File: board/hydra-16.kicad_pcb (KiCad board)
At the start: 2 copper layers, 304.8 x 243.8 mm, 171 parts, among them IC1 74LS189, IC2 74LS189, IC3 74LS189, IC4 74LS189, IC5 74LS219, IC6 74LS219, IC7 74LS219, IC8 74LS219, J1 Conn_01x32, J10 SLOT 1, J11 SLOT 2, J12 SLOT 3, J13 SLOT 4, J14 SLOT 5, J15 AudioJack3, J16 SPI Device 0, J17 Front Panel, J18 SPI Device 1, J19 SPI Device 2, J2 Conn_01x24, J20 SPI Device 3, J21 SPI Device 4, J22 SPI Device 5, J23 SPI Device 6, J24 SPI Device 7, J3 DE9_Plug, J4 7.15909MHz, J5 ATX-24, J6 0.89489MHz, J7 1.78977MHz, J8 3.57955MHz, J9 SLOT 0, U1 74F573, U10 74LS154, U11 74F00, U12 74F86, U13 74F08, U14 74F32, U15 74F30, U16 74LS260, U17 74LS154, U18 74F04, U19 HM628512LP-5, U2 74F541, U20 HM628512LP-5, U21 HM628512LP-5, U22 HM628512LP-5, U23 74F139, U24 74F20, U25 74F02, U26 74LS154, U27 74F138, U28 AT29C040, U29 AT29C040, U3 AT28C64B, U30 AT29C040, U31 AT29C040, U32 AT29C040, U33 AT29C040, U34 AT29C040, U35 AT29C040, U36 74ACT14, U37 74F191, U38 TL074, U39 YM2151, U4 W65C02SxP, U40 YM3012, U41 DM1813-10, U42 74F157, U43 74F157, U44 74LS148, U45 74LS148, U46 74F32, U47 74F573, U48 74F541, U49 74F573, U5 6522, U50 74F541, U51 74F32, U52 74F04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

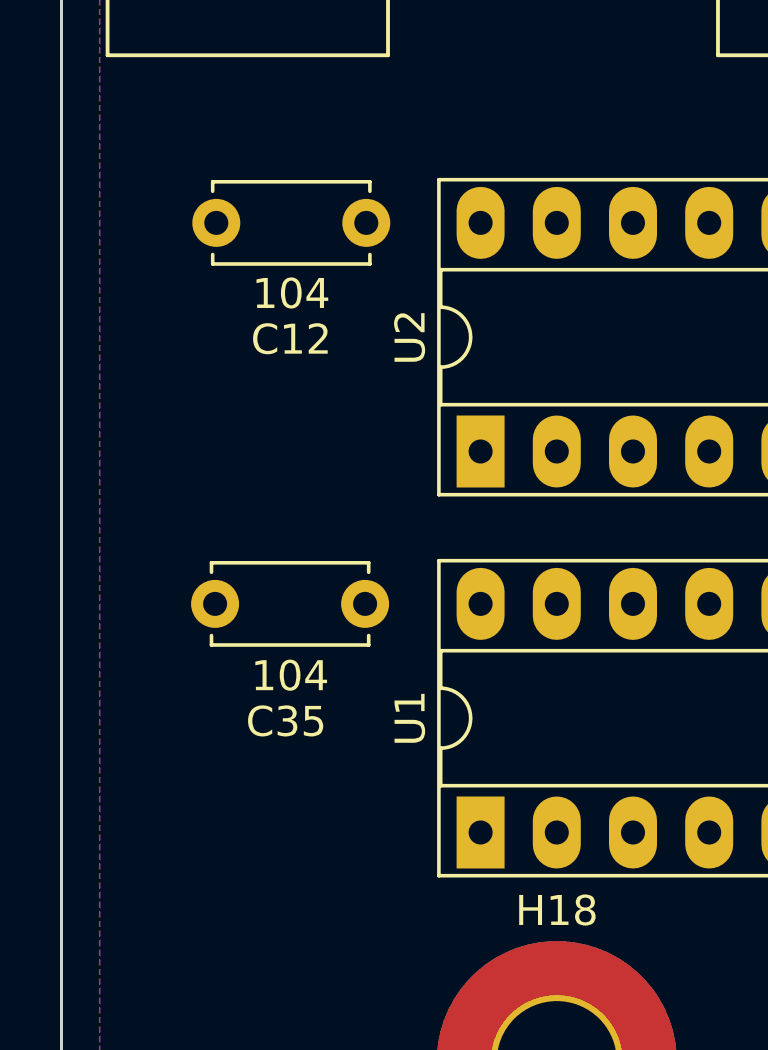
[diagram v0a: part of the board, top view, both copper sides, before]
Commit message: Cap position tweaks.
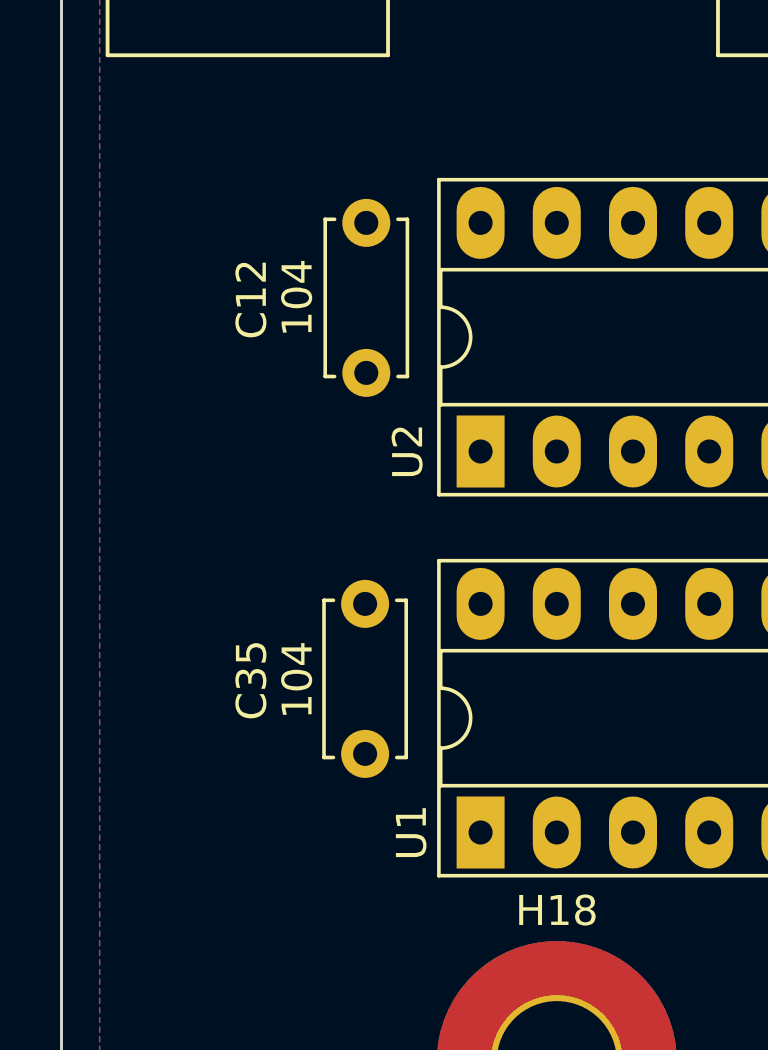
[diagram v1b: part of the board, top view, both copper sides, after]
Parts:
- turned C12 to -90 degrees
- turned C35 to -90 degrees
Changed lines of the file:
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@@
 		(tags "THT DIP DIL PDIP 2.54mm 7.62mm 300mil Socket LongPads")
 		(property "Reference" "U2"
-			(at 3.81 -2.33 90)
+			(at 0 -2.413 90)
 			(layer "F.SilkS")
 			(effects
@@
 	(footprint "Capacitor_THT:C_Disc_D5.0mm_W2.5mm_P5.00mm"
 		(layer "F.Cu")
-		(at -294.64 137.16 180)
+		(at -294.64 137.16 -90)
 		(descr "C, Disc series, Radial, pin pitch=5.00mm, , diameter*width=5*2.5mm^2, Capacitor, http://cdn-reichelt.de/documents/datenblatt/B300/DS_KERKO_TC.pdf")
 		(tags "C Disc series Radial pin pitch 5.00mm  diameter 5mm width 2.5mm Capacitor")
 		(property "Reference" "C12"
-			(at 2.5 -3.897 0)
+			(at 2.54 3.81 90)
 			(layer "F.SilkS")
 			(effects
@@
 		)
 		(property "Value" "104"
-			(at 2.5 -2.373 0)
+			(at 2.5 2.286 90)
 			(layer "F.SilkS")
 			(effects
@@
 		)
 		(property "Footprint" "Capacitor_THT:C_Disc_D5.0mm_W2.5mm_P5.00mm"
-			(at 0 0 180)
+			(at 0 0 -90)
 			(unlocked yes)
 			(layer "F.Fab")
@@
 		)
 		(property "Datasheet" ""
-			(at 0 0 180)
+			(at 0 0 -90)
 			(unlocked yes)
 			(layer "F.Fab")
@@
 		)
 		(property "Description" "Unpolarized capacitor, small symbol"
-			(at 0 0 180)
+			(at 0 0 -90)
 			(unlocked yes)
 			(layer "F.Fab")
@@
 		(attr through_hole)
 		(fp_line
-			(start 5.12 1.055)
+			(start -0.12 1.37)
 			(end 5.12 1.37)
 			(stroke
@@
 		)
 		(fp_line
-			(start 5.12 -1.37)
-			(end 5.12 -1.055)
+			(start -0.12 1.055)
+			(end -0.12 1.37)
 			(stroke
 				(width 0.12)
@@
 		)
 		(fp_line
-			(start -0.12 1.37)
+			(start 5.12 1.055)
 			(end 5.12 1.37)
 			(stroke
@@
 		)
 		(fp_line
-			(start -0.12 1.055)
-			(end -0.12 1.37)
+			(start -0.12 -1.37)
+			(end -0.12 -1.055)
 			(stroke
 				(width 0.12)
@@
 		)
 		(fp_line
-			(start -0.12 -1.37)
-			(end -0.12 -1.055)
+			(start 5.12 -1.37)
+			(end 5.12 -1.055)
 			(stroke
 				(width 0.12)
@@
 		)
 		(fp_line
-			(start 6.05 1.5)
-			(end 6.05 -1.5)
+			(start -1.05 1.5)
+			(end 6.05 1.5)
 			(stroke
 				(width 0.05)
@@
 		)
 		(fp_line
-			(start 6.05 -1.5)
-			(end -1.05 -1.5)
+			(start 6.05 1.5)
+			(end 6.05 -1.5)
 			(stroke
 				(width 0.05)
@@
 		)
 		(fp_line
-			(start -1.05 1.5)
-			(end 6.05 1.5)
+			(start -1.05 -1.5)
+			(end -1.05 1.5)
 			(stroke
 				(width 0.05)
@@
 		)
 		(fp_line
-			(start -1.05 -1.5)
-			(end -1.05 1.5)
+			(start 6.05 -1.5)
+			(end -1.05 -1.5)
 			(stroke
 				(width 0.05)
@@
 		)
 		(fp_line
-			(start 5 1.25)
-			(end 5 -1.25)
+			(start 0 1.25)
+			(end 5 1.25)
 			(stroke
 				(width 0.1)
@@
 		)
 		(fp_line
-			(start 5 -1.25)
-			(end 0 -1.25)
+			(start 5 1.25)
+			(end 5 -1.25)
 			(stroke
 				(width 0.1)
@@
 		)
 		(fp_line
-			(start 0 1.25)
-			(end 5 1.25)
+			(start 0 -1.25)
+			(end 0 1.25)
 			(stroke
 				(width 0.1)
@@
 		)
 		(fp_line
-			(start 0 -1.25)
-			(end 0 1.25)
+			(start 5 -1.25)
+			(end 0 -1.25)
 			(stroke
 				(width 0.1)
@@
 		)
 		(fp_text user "${REFERENCE}"
-			(at 2.5 0 0)
+			(at 2.5 0 90)
 			(layer "F.Fab")
 			(effects
@@
 		)
 		(pad "1" thru_hole circle
-			(at 0 0 180)
+			(at 0 0 270)
 			(size 1.6 1.6)
 			(drill 0.8)
@@
 		)
 		(pad "2" thru_hole circle
-			(at 5 0 180)
+			(at 5 0 270)
 			(size 1.6 1.6)
 			(drill 0.8)
@@
 		(tags "THT DIP DIL PDIP 2.54mm 7.62mm 300mil Socket LongPads")
 		(property "Reference" "U1"
-			(at 3.81 -2.33 90)
+			(at 0 -2.286 90)
 			(layer "F.SilkS")
 			(effects
@@
 	(footprint "Capacitor_THT:C_Disc_D5.0mm_W2.5mm_P5.00mm"
 		(layer "F.Cu")
-		(at -294.68 149.86 180)
+		(at -294.68 149.86 -90)
 		(descr "C, Disc series, Radial, pin pitch=5.00mm, , diameter*width=5*2.5mm^2, Capacitor, http://cdn-reichelt.de/documents/datenblatt/B300/DS_KERKO_TC.pdf")
 		(tags "C Disc series Radial pin pitch 5.00mm  diameter 5mm width 2.5mm Capacitor")
 		(property "Reference" "C35"
-			(at 2.627 -3.937 0)
+			(at 2.54 3.77 90)
 			(layer "F.SilkS")
 			(effects
@@
 		)
 		(property "Value" "104"
-			(at 2.5 -2.413 0)
+			(at 2.54 2.246 90)
 			(layer "F.SilkS")
 			(effects
@@
 		)
 		(property "Footprint" "Capacitor_THT:C_Disc_D5.0mm_W2.5mm_P5.00mm"
-			(at 0 0 180)
+			(at 0 0 -90)
 			(unlocked yes)
 			(layer "F.Fab")
@@
 		)
 		(property "Datasheet" ""
-			(at 0 0 180)
+			(at 0 0 -90)
 			(unlocked yes)
 			(layer "F.Fab")
@@
 		)
 		(property "Description" "Unpolarized capacitor, small symbol"
-			(at 0 0 180)
+			(at 0 0 -90)
 			(unlocked yes)
 			(layer "F.Fab")
@@
 		(attr through_hole)
 		(fp_line
-			(start 5.12 1.055)
+			(start -0.12 1.37)
 			(end 5.12 1.37)
 			(stroke
@@
 		)
 		(fp_line
-			(start 5.12 -1.37)
-			(end 5.12 -1.055)
+			(start -0.12 1.055)
+			(end -0.12 1.37)
 			(stroke
 				(width 0.12)
@@
 		)
 		(fp_line
-			(start -0.12 1.37)
+			(start 5.12 1.055)
 			(end 5.12 1.37)
 			(stroke
@@
 		)
 		(fp_line
-			(start -0.12 1.055)
-			(end -0.12 1.37)
+			(start -0.12 -1.37)
+			(end -0.12 -1.055)
 			(stroke
 				(width 0.12)
@@
 		)
 		(fp_line
-			(start -0.12 -1.37)
-			(end -0.12 -1.055)
+			(start 5.12 -1.37)
+			(end 5.12 -1.055)
 			(stroke
 				(width 0.12)
@@
 		)
 		(fp_line
-			(start 6.05 1.5)
-			(end 6.05 -1.5)
+			(start -1.05 1.5)
+			(end 6.05 1.5)
 			(stroke
 				(width 0.05)
@@
 		)
 		(fp_line
-			(start 6.05 -1.5)
-			(end -1.05 -1.5)
+			(start 6.05 1.5)
+			(end 6.05 -1.5)
 			(stroke
 				(width 0.05)
@@
 		)
 		(fp_line
-			(start -1.05 1.5)
-			(end 6.05 1.5)
+			(start -1.05 -1.5)
+			(end -1.05 1.5)
 			(stroke
 				(width 0.05)
@@
 		)
 		(fp_line
-			(start -1.05 -1.5)
-			(end -1.05 1.5)
+			(start 6.05 -1.5)
+			(end -1.05 -1.5)
 			(stroke
 				(width 0.05)
@@
 		)
 		(fp_line
-			(start 5 1.25)
-			(end 5 -1.25)
+			(start 0 1.25)
+			(end 5 1.25)
 			(stroke
 				(width 0.1)
@@
 		)
 		(fp_line
-			(start 5 -1.25)
-			(end 0 -1.25)
+			(start 5 1.25)
+			(end 5 -1.25)
 			(stroke
 				(width 0.1)
@@
 		)
 		(fp_line
-			(start 0 1.25)
-			(end 5 1.25)
+			(start 0 -1.25)
+			(end 0 1.25)
 			(stroke
 				(width 0.1)
@@
 		)
 		(fp_line
-			(start 0 -1.25)
-			(end 0 1.25)
+			(start 5 -1.25)
+			(end 0 -1.25)
 			(stroke
 				(width 0.1)
@@
 		)
 		(fp_text user "${REFERENCE}"
-			(at 2.5 0 0)
+			(at 2.5 0 90)
 			(layer "F.Fab")
 			(effects
@@
 		)
 		(pad "1" thru_hole circle
-			(at 0 0 180)
+			(at 0 0 270)
 			(size 1.6 1.6)
 			(drill 0.8)
@@
 		)
 		(pad "2" thru_hole circle
-			(at 5 0 180)
+			(at 5 0 270)
 			(size 1.6 1.6)
 			(drill 0.8)

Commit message: More PCB position tweaks.
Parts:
- RN2: value 3.3k -> 332
- U4: value W65C02SxP -> W65C02S
- U5: value 6522 -> 65C22
- U6: value 6551 -> 65C51
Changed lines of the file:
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@@
 		(tags "THT DIP DIL PDIP 2.54mm 7.62mm 300mil Socket LongPads")
 		(property "Reference" "IC2"
-			(at -0.1455 -2.4839 180)
+			(at 3.7915 21.7731 180)
 			(layer "F.SilkS")
 			(effects
@@
 			)
 		)
-		(property "Value" "W65C02SxP"
+		(property "Value" "W65C02S"
 			(at 7.62 50.59 180)
 			(layer "F.SilkS")
@@
 			)
 		)
-		(property "Value" "6551"
+		(property "Value" "65C51"
 			(at 7.62 35.35 0)
 			(layer "F.SilkS")
@@
 		(tags "THT DIP DIL PDIP 2.54mm 7.62mm 300mil Socket LongPads")
 		(property "Reference" "U23"
-			(at -0.381 -2.667 0)
+			(at 3.673 21.854 0)
 			(layer "F.SilkS")
 			(effects
@@
 		(tags "R")
 		(property "Reference" "RN2"
-			(at -2.794 0 180)
+			(at -4.064 0 180)
 			(layer "F.SilkS")
 			(effects
@@
 			)
 		)
-		(property "Value" "3.3k"
-			(at 22.86 0 180)
+		(property "Value" "332"
+			(at -2.54 0 180)
 			(layer "F.SilkS")
 			(effects
@@
 		(tags "R")
 		(property "Reference" "RN3"
-			(at -2.794 0 180)
+			(at -4.064 0 180)
 			(layer "F.SilkS")
 			(effects
@@
 		)
 		(property "Value" "332"
-			(at 22.86 0 180)
+			(at -2.54 0 180)
 			(layer "F.SilkS")
 			(effects
@@
 		(tags "R")
 		(property "Reference" "RN1"
-			(at 11.43 4.064 90)
+			(at 10.16 4.064 90)
 			(layer "F.SilkS")
 			(effects
@@
 		)
 		(property "Value" "332"
-			(at 11.43 2.413 90)
+			(at 10.16 2.413 90)
 			(layer "F.SilkS")
 			(effects
@@
 			)
 		)
-		(property "Value" "6522"
+		(property "Value" "65C22"
 			(at 7.62 50.59 180)
 			(layer "F.SilkS")

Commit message: More PCB position tweaks.
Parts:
- turned C41 to 0 degrees
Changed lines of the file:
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@@
 	(footprint "Capacitor_THT:C_Disc_D5.0mm_W2.5mm_P5.00mm"
 		(layer "F.Cu")
-		(at -261.62 138.43 90)
+		(at -261.62 138.43)
 		(descr "C, Disc series, Radial, pin pitch=5.00mm, , diameter*width=5*2.5mm^2, Capacitor, http://cdn-reichelt.de/documents/datenblatt/B300/DS_KERKO_TC.pdf")
 		(tags "C Disc series Radial pin pitch 5.00mm  diameter 5mm width 2.5mm Capacitor")
 		(property "Reference" "C41"
-			(at 2.413 3.81 90)
+			(at 2.413 -3.81 360)
 			(layer "F.SilkS")
 			(effects
@@
 		)
 		(property "Value" "104"
-			(at 2.54 2.286 90)
+			(at 2.54 -2.286 360)
 			(layer "F.SilkS")
 			(effects
@@
 		)
 		(property "Footprint" "Capacitor_THT:C_Disc_D5.0mm_W2.5mm_P5.00mm"
-			(at 0 0 90)
+			(at 0 0 0)
 			(unlocked yes)
 			(layer "F.Fab")
@@
 		)
 		(property "Datasheet" ""
-			(at 0 0 90)
+			(at 0 0 0)
 			(unlocked yes)
 			(layer "F.Fab")
@@
 		)
 		(property "Description" "Unpolarized capacitor, small symbol"
-			(at 0 0 90)
+			(at 0 0 0)
 			(unlocked yes)
 			(layer "F.Fab")
@@
 		(attr through_hole)
 		(fp_line
-			(start 5.12 -1.37)
-			(end 5.12 -1.055)
+			(start -0.12 -1.37)
+			(end -0.12 -1.055)
 			(stroke
 				(width 0.12)
@@
 		)
 		(fp_line
-			(start -0.12 -1.37)
-			(end -0.12 -1.055)
+			(start -0.12 1.055)
+			(end -0.12 1.37)
 			(stroke
 				(width 0.12)
@@
 		)
 		(fp_line
-			(start 5.12 1.055)
+			(start -0.12 1.37)
 			(end 5.12 1.37)
 			(stroke
@@
 		)
 		(fp_line
-			(start -0.12 1.055)
-			(end -0.12 1.37)
+			(start 5.12 -1.37)
+			(end 5.12 -1.055)
 			(stroke
 				(width 0.12)
@@
 		)
 		(fp_line
-			(start -0.12 1.37)
+			(start 5.12 1.055)
 			(end 5.12 1.37)
 			(stroke
@@
 		)
 		(fp_line
-			(start 6.05 -1.5)
-			(end -1.05 -1.5)
+			(start -1.05 -1.5)
+			(end -1.05 1.5)
 			(stroke
 				(width 0.05)
@@
 		)
 		(fp_line
-			(start -1.05 -1.5)
-			(end -1.05 1.5)
+			(start -1.05 1.5)
+			(end 6.05 1.5)
 			(stroke
 				(width 0.05)
@@
 		)
 		(fp_line
-			(start 6.05 1.5)
-			(end 6.05 -1.5)
+			(start 6.05 -1.5)
+			(end -1.05 -1.5)
 			(stroke
 				(width 0.05)
@@
 		)
 		(fp_line
-			(start -1.05 1.5)
-			(end 6.05 1.5)
+			(start 6.05 1.5)
+			(end 6.05 -1.5)
 			(stroke
 				(width 0.05)
@@
 		)
 		(fp_line
-			(start 5 -1.25)
-			(end 0 -1.25)
+			(start 0 -1.25)
+			(end 0 1.25)
 			(stroke
 				(width 0.1)
@@
 		)
 		(fp_line
-			(start 0 -1.25)
-			(end 0 1.25)
+			(start 0 1.25)
+			(end 5 1.25)
 			(stroke
 				(width 0.1)
@@
 		)
 		(fp_line
-			(start 5 1.25)
-			(end 5 -1.25)
+			(start 5 -1.25)
+			(end 0 -1.25)
 			(stroke
 				(width 0.1)
@@
 		)
 		(fp_line
-			(start 0 1.25)
-			(end 5 1.25)
+			(start 5 1.25)
+			(end 5 -1.25)
 			(stroke
 				(width 0.1)
@@
 		)
 		(fp_text user "${REFERENCE}"
-			(at 2.5 0 90)
+			(at 2.5 0 360)
 			(layer "F.Fab")
 			(effects
@@
 		)
 		(pad "1" thru_hole circle
-			(at 0 0 90)
+			(at 0 0)
 			(size 1.6 1.6)
 			(drill 0.8)
@@
 		)
 		(pad "2" thru_hole circle
-			(at 5 0 90)
+			(at 5 0)
 			(size 1.6 1.6)
 			(drill 0.8)
@@
 		(tags "THT DIP DIL PDIP 2.54mm 7.62mm 300mil Socket LongPads")
 		(property "Reference" "U2"
-			(at 0 -2.413 90)
+			(at 3.683 26.67 90)
 			(layer "F.SilkS")
 			(effects
@@
 		(tags "THT DIP DIL PDIP 2.54mm 7.62mm 300mil Socket LongPads")
 		(property "Reference" "U1"
-			(at 0 -2.286 90)
+			(at 3.937 26.67 90)
 			(layer "F.SilkS")
 			(effects
@@
 		(tags "THT DIP DIL PDIP 2.54mm 15.24mm 600mil Socket LongPads")
 		(property "Reference" "U10"
-			(at 7.62 -2.33 90)
+			(at 7.62 31.75 90)
 			(layer "F.SilkS")
 			(effects
